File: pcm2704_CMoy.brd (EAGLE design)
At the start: 100.3 x 77.5 mm, 85 parts, among them IC3 7815DT, IC4 tsr 1-2433, IC5 7915TV, Q1 12MHz, U1 PCM2704, U2 OPA2134P, U3 TC962EPA, X2 PN61729-S, X5 22-23-2031, X6 22-23-2031

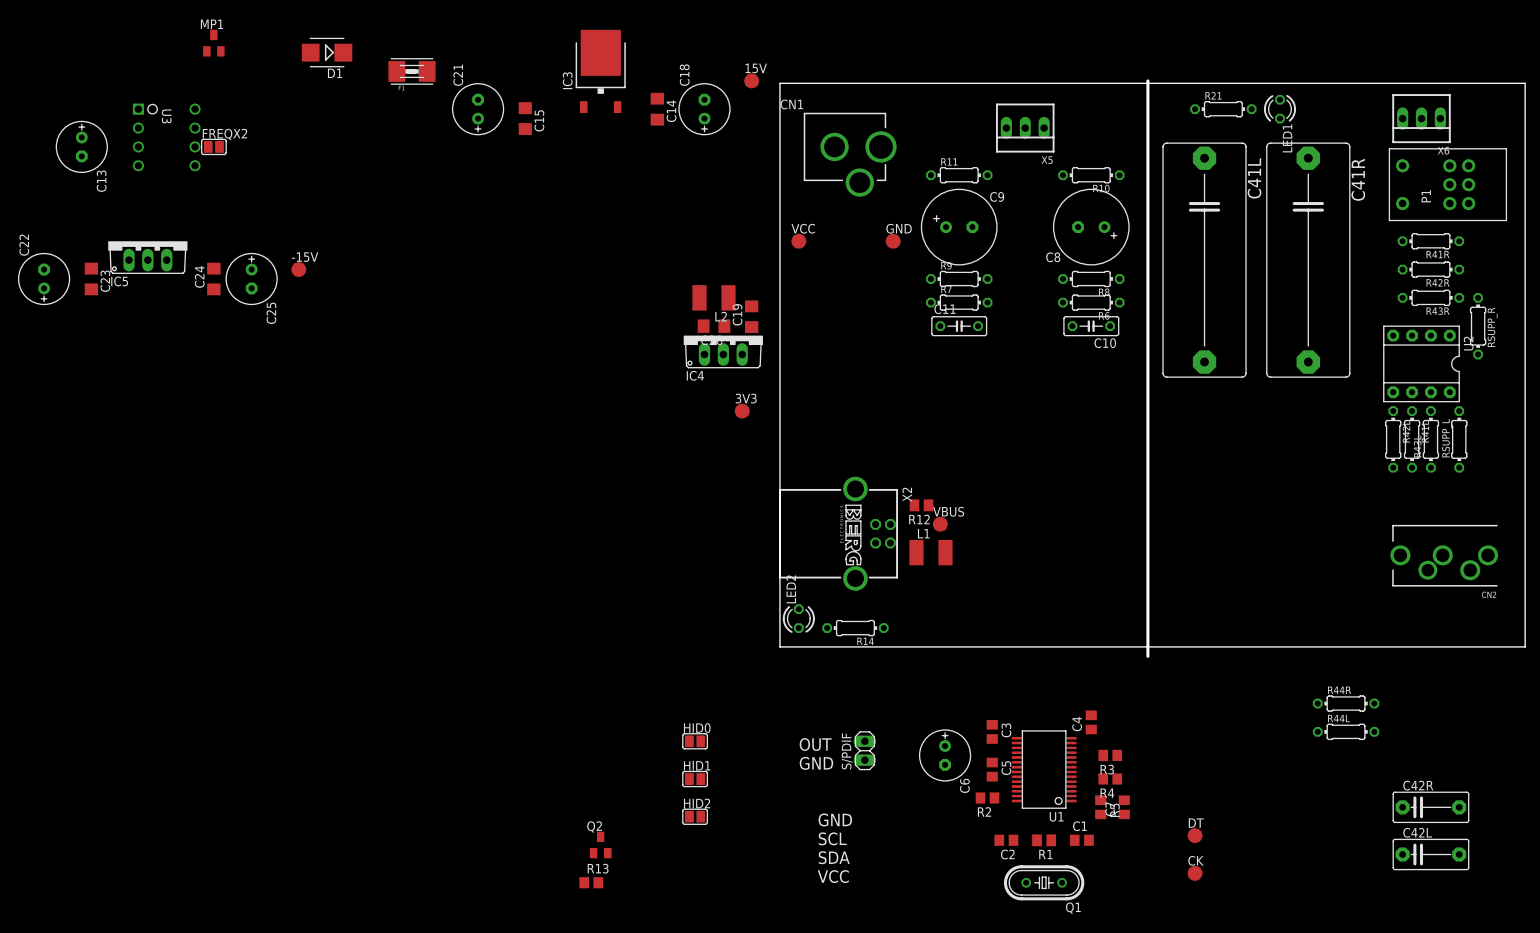
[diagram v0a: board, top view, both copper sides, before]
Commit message: - Added resistor between the wiper and ground of the volume pot
 - Fixed the pot direction
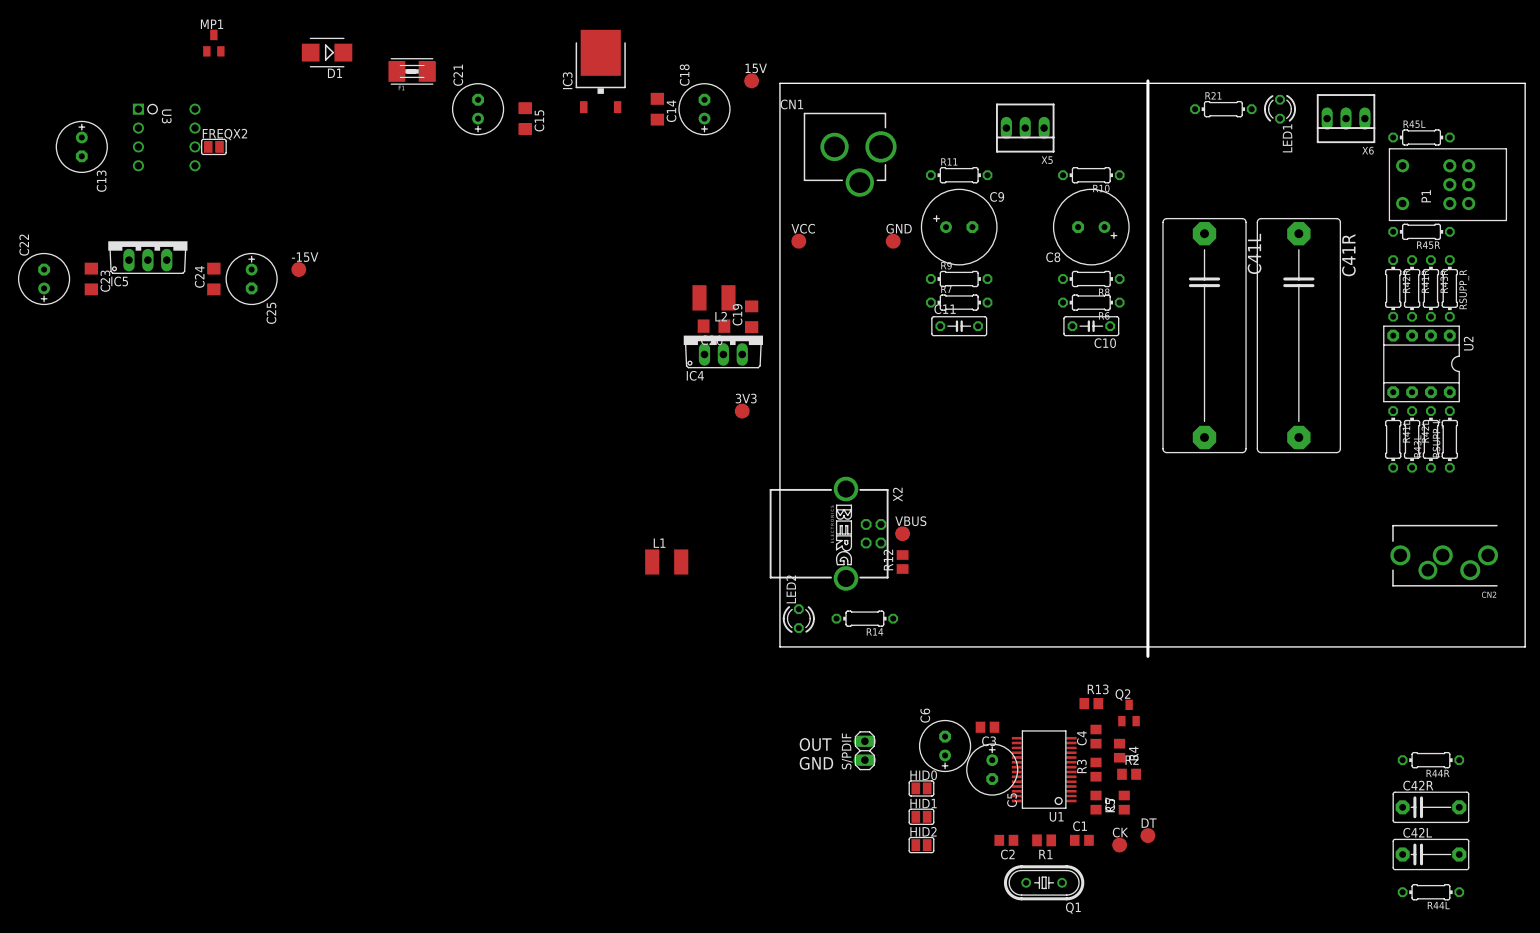
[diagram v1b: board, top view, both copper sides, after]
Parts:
- added R45L, R45R: 1M, rcl:0204/7
- C5: device rcl:C0805 -> qfm-trx1-24g:E2,5-7
- moved Q2 73.3 mm to (47.0, -8.89)
- moved R13 71.5 mm to (41.9, -7.62)
- moved L1 35.6 mm to (-15.2, 11.4)
- moved HID0 31.1 mm to (19.1, -19.1)
- moved HID1 30.9 mm to (19.1, -22.9)
- moved HID2 30.7 mm to (19.1, -26.7)
- moved R44L 24.4 mm to (87.6, -33.0), turned to 180 degrees
- moved R2 19.3 mm to (47.0, -17.1), turned to 0 degrees
- moved R44R 13.7 mm to (87.6, -15.2), turned to 180 degrees
- moved CK 10.9 mm to (45.7, -26.7)
- moved C41R 10.2 mm to (69.8, 41.9)
- moved C41L 10.2 mm to (57.1, 41.9)
- moved X6 10.2 mm to (76.2, 71.1)
- moved R12 8.03 mm to (16.5, 11.4), turned to 90 degrees
- moved R41R 6.84 mm to (85.1, 48.3), turned to 270 degrees
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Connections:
- net +3V3: now also C5.+; no longer C5.2
- net DAC_OUT_LEFT: now also P1.I1; no longer P1.G1
- net DAC_OUT_RIGHT: now also P1.I2; no longer P1.G2
- net GND: now also C5.-, P1.G1, P1.G2, R45L.1, R45R.1; no longer C5.1, P1.I1, P1.I2
- net N$19: now also R45R.2
- net N$21: now also R45L.2
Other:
- board text removed: "SCL"
- board text removed: "SDA"
- board text removed: "VCC"
